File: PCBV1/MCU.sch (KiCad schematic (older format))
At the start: 41 parts, among them J4 20021121-00010C4LF, U4 STM32F469IITx, X1 ECS-5032MV-100-BN-TR

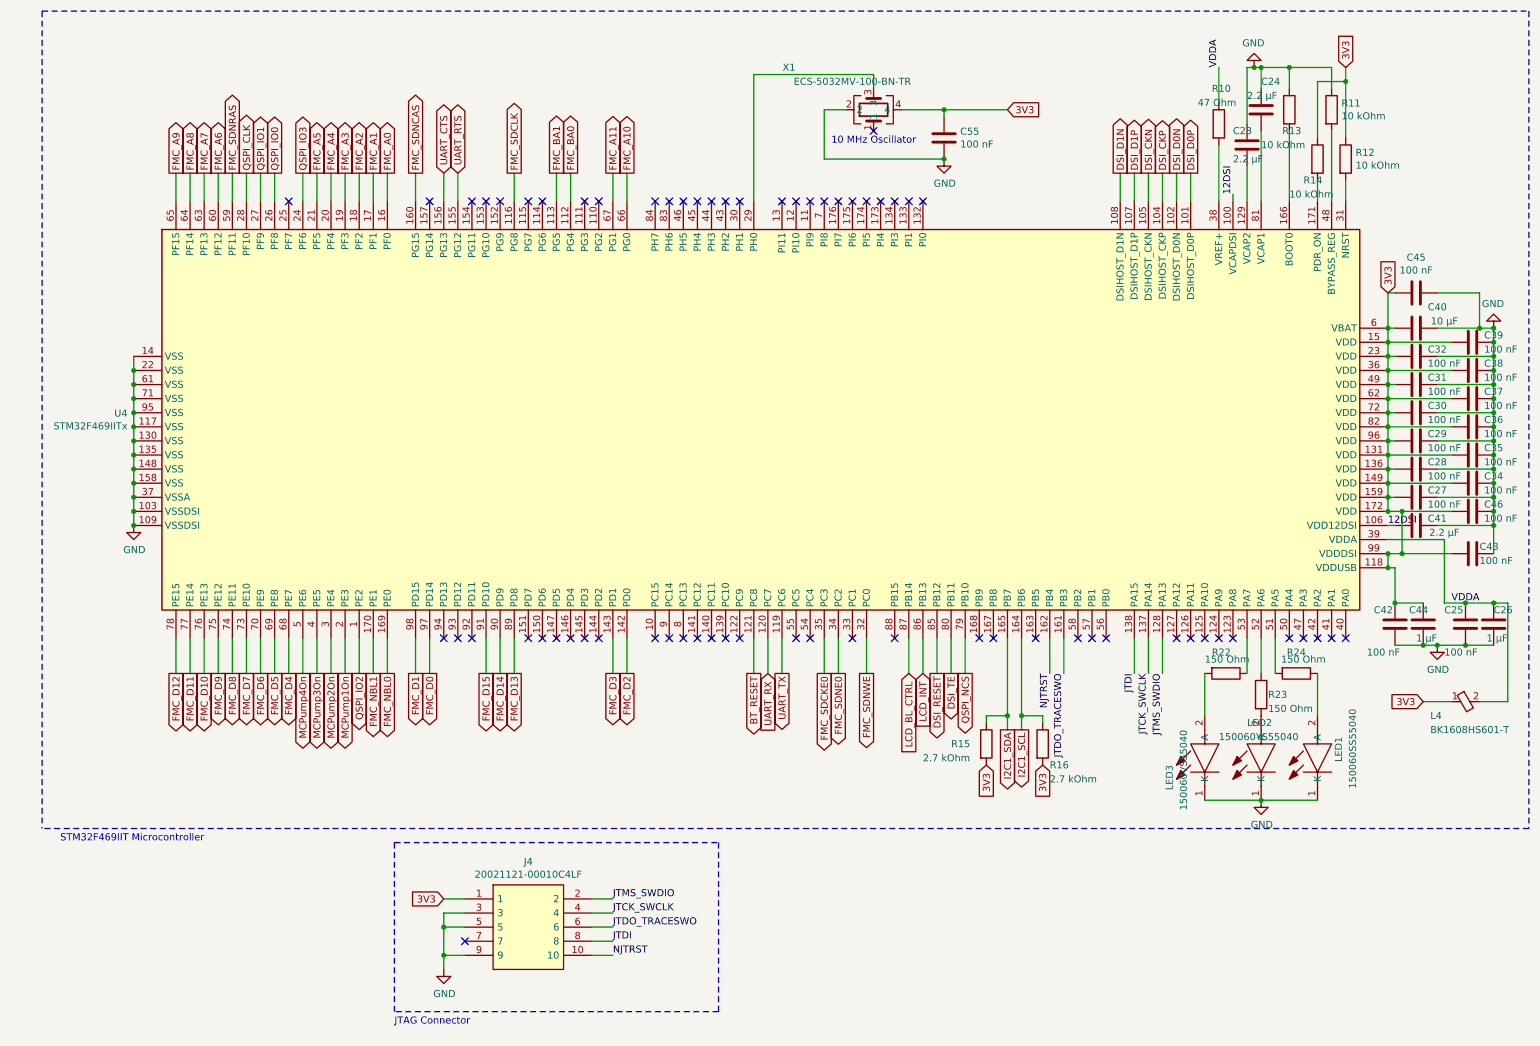
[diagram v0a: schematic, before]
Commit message: Changed ferrite beads to ones with adequate max currents. Changed JTAG connector to 20-pin standard. Minor PCB fixes.
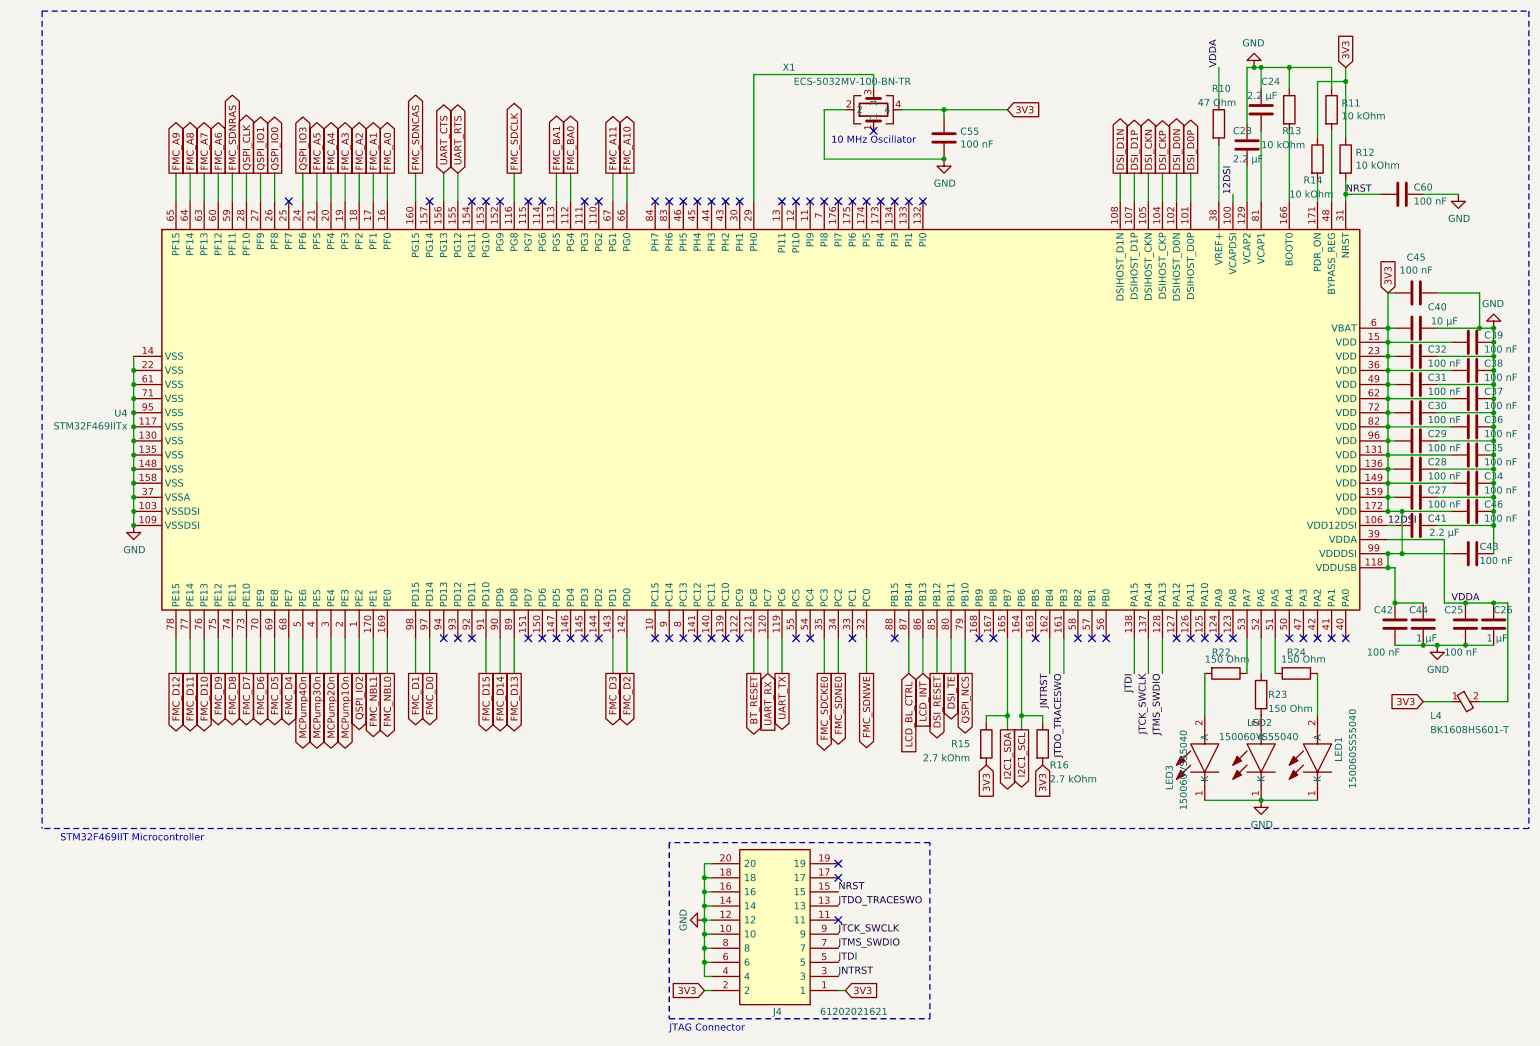
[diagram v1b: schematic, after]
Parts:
- removed J4: 20021121-00010C4LF, HUSSP10W40P127_2X5_635X340X420P, symbol SamacSys_Parts:M50-3600542R
- added C60: 100 nF, Capacitor_SMD:C_0603_1608Metric, symbol Device:C
- added J4: 61202021621, SHDR20W64P254_2X10_3306X910X885P, symbol SamacSys_Parts:61202021621
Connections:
- net 3V3: now also J4.1, J4.2
- net GND: now also C60.1, J4.10, J4.12, J4.14, J4.16, J4.18, J4.20, J4.4, J4.6, J4.8
- net JTCK_SWCLK: now also J4.9
- net JTDI: now also J4.5
- net JTDO_TRACESWO: now also J4.13
- net JTMS_SWDIO: now also J4.7
- net NRST: now reaches R12.2, U4.31 (NRST)
- net NRST: now also C60.2, J4.15
- net NJTRST renamed JNTRST
- net JNTRST: now also J4.3
- no-connect marks 65 -> 67
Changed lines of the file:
@@
 	9700 950  9400 950
 Wire Wire Line
-	9800 1900 9800 1750
+	9800 1900 9800 1850
 $Comp
 L Device:R R12
@@
 JTDO_TRACESWO
 Text Label 7700 5250 3    50   ~ 0
-NJTRST
+JNTRST
 Wire Wire Line
 	9600 1900 9600 1750
@@
 Text GLabel 10350 5450 0    50   Input ~ 0
 3V3
-$Comp
-L SamacSys_Parts:M50-3600542R J4
-U 1 1 5F3832B7
-P 3550 6850
-F 0 "J4" H 4000 7115 50  0000 C CNN
-F 1 "20021121-00010C4LF" H 4000 7024 50  0000 C CNN
-F 2 "HUSSP10W40P127_2X5_635X340X420P" H 4300 6950 50  0001 L CNN
-F 3 "https://www.mouser.dk/ProductDetail/Amphenol-FCI/20021121-00010C4LF?qs=%2Fha2pyFaduhk6vEDe5a0MwjRWUz4Zk9Fskpe5qL0Xo%2FyZkFkIBBW%2FlKXwnPu0N9C" H 4300 6850 50  0001 L CNN
-F 4 "Amphenol Header" H 4300 6750 50  0001 L CNN "Description"
-F 5 "" H 4300 6650 50  0001 L CNN "Height"
-F 6 " 649-202112100010C4LF" H 4300 6550 50  0001 L CNN "Mouser Part Number"
-F 7 "https://www.mouser.dk/ProductDetail/Amphenol-FCI/20021121-00010C4LF?qs=%2Fha2pyFaduhk6vEDe5a0MwjRWUz4Zk9Fskpe5qL0Xo%2FyZkFkIBBW%2FlKXwnPu0N9C" H 4300 6450 50  0001 L CNN "Mouser Price/Stock"
-F 8 "Amphenol" H 4300 6350 50  0001 L CNN "Manufacturer_Name"
-F 9 "20021121-00010C4LF" H 4300 6250 50  0001 L CNN "Manufacturer_Part_Number"
-	1    3550 6850
-	1    0    0    -1
-$EndComp
-Wire Wire Line
-	3550 6850 3400 6850
-Wire Wire Line
-	3550 6950 3400 6950
-Wire Wire Line
-	3550 7050 3400 7050
-Wire Wire Line
-	3550 7250 3400 7250
-Wire Wire Line
-	4450 6850 4600 6850
-Wire Wire Line
-	4450 6950 4600 6950
-Wire Wire Line
-	4450 7050 4600 7050
-Wire Wire Line
-	4450 7150 4600 7150
-Wire Wire Line
-	4450 7250 4600 7250
-NoConn ~ 3550 7150
-Text GLabel 3400 6850 0    50   Input ~ 0
-3V3
-Wire Wire Line
-	3400 6950 3400 7050
-Connection ~ 3400 7050
-Wire Wire Line
-	3400 7050 3400 7250
-Connection ~ 3400 7250
-Wire Wire Line
-	3400 7250 3400 7350
-$Comp
-L power:GND #PWR0127
-U 1 1 5F3B7270
-P 3400 7350
-F 0 "#PWR0127" H 3400 7100 50  0001 C CNN
-F 1 "GND" H 3405 7177 50  0000 C CNN
-F 2 "" H 3400 7350 50  0001 C CNN
-F 3 "" H 3400 7350 50  0001 C CNN
-	1    3400 7350
-	1    0    0    -1
-$EndComp
-Text Label 4600 7250 0    50   ~ 0
-NJTRST
-Text Label 4600 7150 0    50   ~ 0
+Text Label 6200 7400 0    50   ~ 0
+JNTRST
+Text Label 6200 7300 0    50   ~ 0
 JTDI
-Text Label 4600 7050 0    50   ~ 0
+Text Label 6200 6900 0    50   ~ 0
 JTDO_TRACESWO
-Text Label 4600 6950 0    50   ~ 0
+Text Label 6200 7100 0    50   ~ 0
 JTCK_SWCLK
-Text Label 4600 6850 0    50   ~ 0
+Text Label 6200 7200 0    50   ~ 0
 JTMS_SWDIO
-Wire Notes Line
-	3050 7650 3050 6450
-Wire Notes Line
-	3050 6450 5350 6450
-Wire Notes Line
-	5350 6450 5350 7650
-Wire Notes Line
-	5350 7650 3050 7650
-Text Notes 3050 7750 0    50   ~ 0
+Text Notes 5000 7800 0    50   ~ 0
 JTAG Connector
 Wire Wire Line
@@
 Wire Wire Line
 	6950 1250 7400 1250
+$Comp
+L SamacSys_Parts:61202021621 J4
+U 1 1 5F976C7D
+P 6200 7500
+F 0 "J4" H 6600 7650 50  0000 L CNN
+F 1 "61202021621" H 5850 7650 50  0000 L CNN
+F 2 "SHDR20W64P254_2X10_3306X910X885P" H 6950 7600 50  0001 L CNN
+F 3 "" H 6950 7500 50  0001 L CNN
+F 4 "Wurth Elektronik 612 Series, 2.54mm Pitch 20 Way 2 Row Straight PCB Header, Solder Termination, 3A" H 6950 7400 50  0001 L CNN "Description"
+F 5 "8.85" H 6950 7300 50  0001 L CNN "Height"
+F 6 "710-61202021621" H 6950 7200 50  0001 L CNN "Mouser Part Number"
+F 7 "https://www.mouser.co.uk/ProductDetail/Wurth-Elektronik/61202021621?qs=ZtY9WdtwX56vYmz0%252BUtUhA%3D%3D" H 6950 7100 50  0001 L CNN "Mouser Price/Stock"
+F 8 "Wurth Elektronik" H 6950 7000 50  0001 L CNN "Manufacturer_Name"
+F 9 "61202021621" H 6950 6900 50  0001 L CNN "Manufacturer_Part_Number"
+	1    6200 7500
+	-1   0    0    1
+$EndComp
+NoConn ~ 6200 7000
+NoConn ~ 6200 6700
+NoConn ~ 6200 6600
+$Comp
+L power:GND #PWR?
+U 1 1 5F9BD06D
+P 5250 7000
+F 0 "#PWR?" H 5250 6750 50  0001 C CNN
+F 1 "GND" H 5250 6850 50  0000 C CNN
+F 2 "" H 5250 7000 50  0001 C CNN
+F 3 "" H 5250 7000 50  0001 C CNN
+	1    5250 7000
+	0    1    1    0
+$EndComp
+Wire Wire Line
+	5250 7400 5250 7300
+Wire Wire Line
+	5250 7300 5300 7300
+Wire Wire Line
+	5250 7300 5250 7200
+Wire Wire Line
+	5250 7200 5300 7200
+Connection ~ 5250 7300
+Wire Wire Line
+	5300 7100 5250 7100
+Wire Wire Line
+	5250 7100 5250 7200
+Connection ~ 5250 7200
+Wire Wire Line
+	5300 7000 5250 7000
+Wire Wire Line
+	5250 7000 5250 7100
+Connection ~ 5250 7100
+Wire Wire Line
+	5300 6900 5250 6900
+Wire Wire Line
+	5250 6900 5250 7000
+Connection ~ 5250 7000
+Wire Wire Line
+	5300 6800 5250 6800
+Wire Wire Line
+	5250 6800 5250 6900
+Connection ~ 5250 6900
+Wire Wire Line
+	5300 6700 5250 6700
+Wire Wire Line
+	5250 6700 5250 6800
+Connection ~ 5250 6800
+Wire Wire Line
+	5300 6600 5250 6600
+Wire Wire Line
+	5250 6600 5250 6700
+Connection ~ 5250 6700
+Wire Wire Line
+	5300 7400 5250 7400
+Text GLabel 6250 7500 2    50   Input ~ 0
+3V3
+Text GLabel 5250 7500 0    50   Input ~ 0
+3V3
+Wire Wire Line
+	5250 7500 5300 7500
+Wire Wire Line
+	6200 7500 6250 7500
+Text Label 6200 6800 0    50   ~ 0
+NRST
+Text Label 9800 1850 0    50   ~ 0
+NRST
+$Comp
+L Device:C C60
+U 1 1 5FAFA95B
+P 10200 1850
+F 0 "C60" V 10150 2000 50  0000 C CNN
+F 1 "100 nF" V 10250 2050 50  0000 C CNN
+F 2 "Capacitor_SMD:C_0603_1608Metric" H 10238 1700 50  0001 C CNN
+F 3 "~" H 10200 1850 50  0001 C CNN
+	1    10200 1850
+	0    1    1    0
+$EndComp
+Wire Wire Line
+	9800 1850 10050 1850
+Connection ~ 9800 1850
+Wire Wire Line
+	9800 1850 9800 1750
+$Comp
+L power:GND #PWR?
+U 1 1 5FB1FA68
+P 10600 1850
+F 0 "#PWR?" H 10600 1600 50  0001 C CNN
+F 1 "GND" H 10605 1677 50  0000 C CNN
+F 2 "" H 10600 1850 50  0001 C CNN
+F 3 "" H 10600 1850 50  0001 C CNN
+	1    10600 1850
+	1    0    0    -1
+$EndComp
+Wire Wire Line
+	10350 1850 10600 1850
+Wire Notes Line
+	5000 7700 6850 7700
+Wire Notes Line
+	6850 7700 6850 6450
+Wire Notes Line
+	6850 6450 5000 6450
+Wire Notes Line
+	5000 6450 5000 7700
 $EndSCHEMATC

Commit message: Added new JTAG/UART header with connections for STLink V3. Moved from SamacSys to personal GitHub-based library.
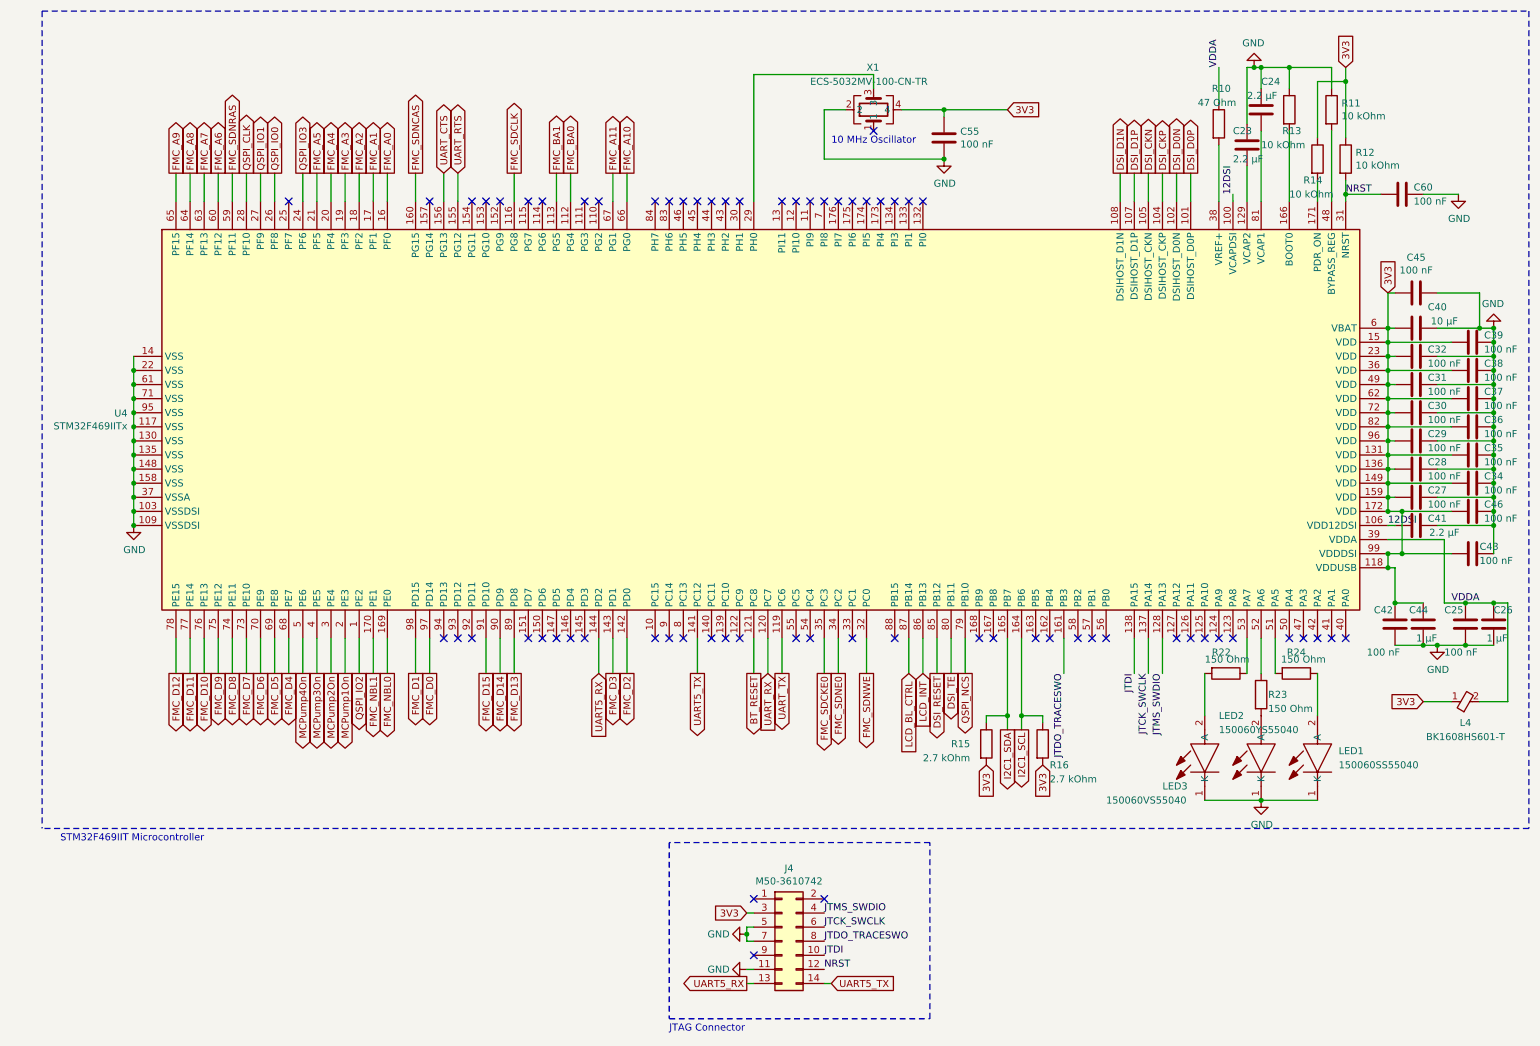
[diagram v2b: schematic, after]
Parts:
- removed J4: 61202021621, SHDR20W64P254_2X10_3306X910X885P, symbol SamacSys_Parts:61202021621
- removed L4: BK1608HS601-T, BEADC1608X95N, symbol SamacSys_Parts:BK1608HS601-T
- removed LED1: 150060SS55040, 150060SS55040, symbol SamacSys_Parts:150060SS55040
- removed LED2: 150060YS55040, 150060SS55040, symbol SamacSys_Parts:150060SS55040
- removed LED3: 150060VS55040, SamacSys_Parts:150060SS55040, symbol SamacSys_Parts:150060VS55040
- removed X1: ECS-5032MV-100-BN-TR, ECS5032MV250CNTR, symbol SamacSys_Parts:ECS-5032MV-250-CN-TR
- added J4: M50-3610742, Personal_Misc:M50-3610742R, symbol Connector_Generic:Conn_02x07_Odd_Even
- added L4: BK1608HS601-T, Personal_Passives:BK1608HS601-T, symbol Personal_Passives:BK1608HS601-T
- added LED1: 150060SS55040, Personal_Passives:150060SS55040, symbol Personal_Passives:150060SS55040
- added LED2: 150060YS55040, Personal_Passives:150060VS55040, symbol Personal_Passives:150060YS55040
- added LED3: 150060VS55040, Personal_Passives:150060VS55040, symbol Personal_Passives:150060VS55040
- added X1: ECS-5032MV-100-CN-TR, Personal_Actives:ECS5032MV250CNTR, symbol Personal_Actives:ECS-5032MV-100-CN-TR
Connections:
- net 3V3: now also J4.3 (Pin_3), L4.1, X1.4
- net GND: now also J4.11 (Pin_11), J4.5 (Pin_5), J4.7 (Pin_7), LED1.1 (K), LED2.1 (K), LED3.1 (K), X1.2
- net JTCK_SWCLK: now also J4.6 (Pin_6)
- net JTDI: now also J4.10 (Pin_10)
- net JTDO_TRACESWO: now also J4.8 (Pin_8)
- net JTMS_SWDIO: now also J4.4 (Pin_4)
- net NRST: now also J4.12 (Pin_12)
- net VDDA: now also L4.2
- net at U4.29 (PH0): now also X1.3
- net at R24.1: now also LED1.2 (A)
- net at R23.2: now also LED2.2 (A)
- net at R22.2: now also LED3.2 (A)
- net UART5_TX: now reaches U4.141 (PC12)
- net UART5_TX: now also J4.14 (Pin_14)
- net UART5_RX: now reaches U4.144 (PD2)
- net UART5_RX: now also J4.13 (Pin_13)
- net JNTRST: no longer names the net of U4.162 (PB4)
- no-connect marks 67 -> 66
